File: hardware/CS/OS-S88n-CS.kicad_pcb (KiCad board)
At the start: 2 copper layers, 105.5 x 63.5 mm, 108 parts, among them J101 Screw_Terminal_01x03, J102 Screw_Terminal_01x03, J103 Screw_Terminal_01x03, J104 Screw_Terminal_01x03, J105 Screw_Terminal_01x03, J106 Screw_Terminal_01x03, J2101 RJ45, J2102 RJ45, Q2101 BC847, U1001 EL814, U1101 EL814, U1301 EL814, U1401 EL814, U1501 EL814, U1601 EL814, U1701 EL814, U1801 EL814, U1901 EL814, U2001 4014, U2002 4014, U201 EL814, U401 EL814, U501 EL814, U601 EL814, U701 EL814, U801 EL814, U901 EL814

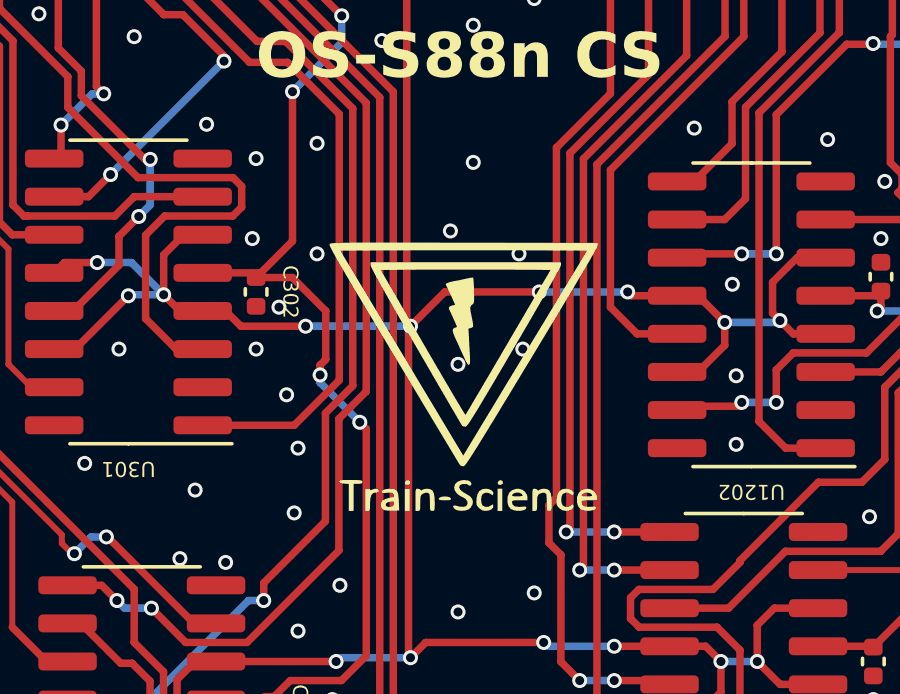
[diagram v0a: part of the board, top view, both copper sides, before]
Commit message: Major overhaul, added the OS-S88n-OPTO, reorganized release files and documentation
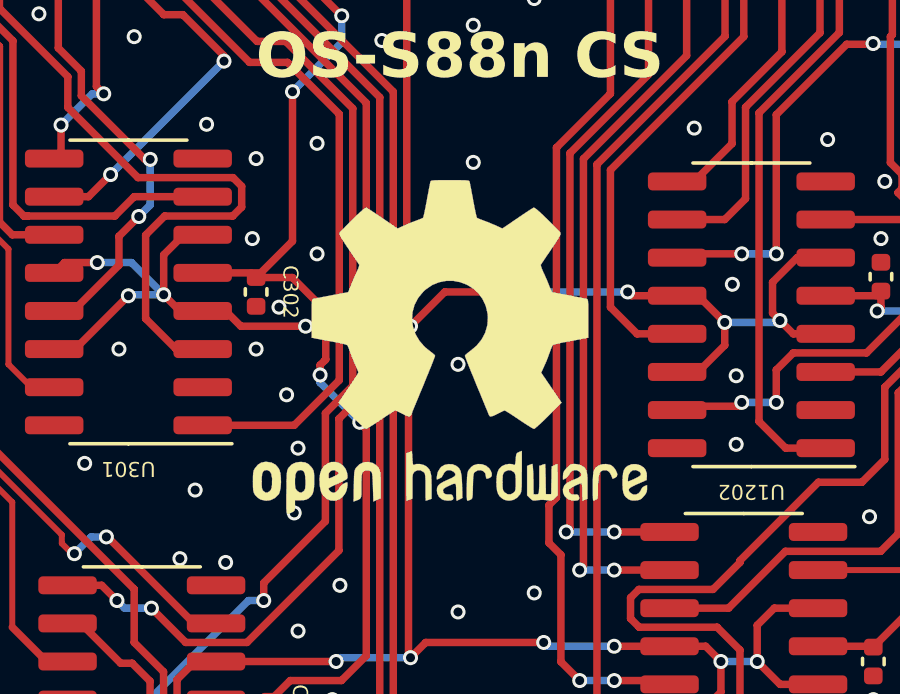
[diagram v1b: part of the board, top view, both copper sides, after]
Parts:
- removed G*** (x2): LOGO, custom_kicad_lib_sk:Train-Science logo small
- added REF**: OSHW-Logo2_14.6x12mm_SilkScreen, Symbol:OSHW-Logo2_14.6x12mm_SilkScreen, F.Cu at (163.5, 100.5)
